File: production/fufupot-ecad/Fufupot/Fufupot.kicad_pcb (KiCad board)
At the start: 4 copper layers, 127 x 127 mm, 56 parts, among them IC1 FOD3150, J1 Conn_01x04, J10 Conn_01x03, J11 Conn_01x03, J12 Conn_01x02, J13 Conn_01x03, J2 USB_B, J3 Conn_01x03, J4 Conn_01x02, J6 Conn_01x02, J7 Conn_01x02, J8 Conn_01x04, J9 Conn_01x02, SW1 SW_Push, SW2 SW_Push, U1 USBLC6-2SC6, U2 LM5165DRC, U3 FT232RL, U4 ATMEGA328P-PN, U5 STGP8NC60KD

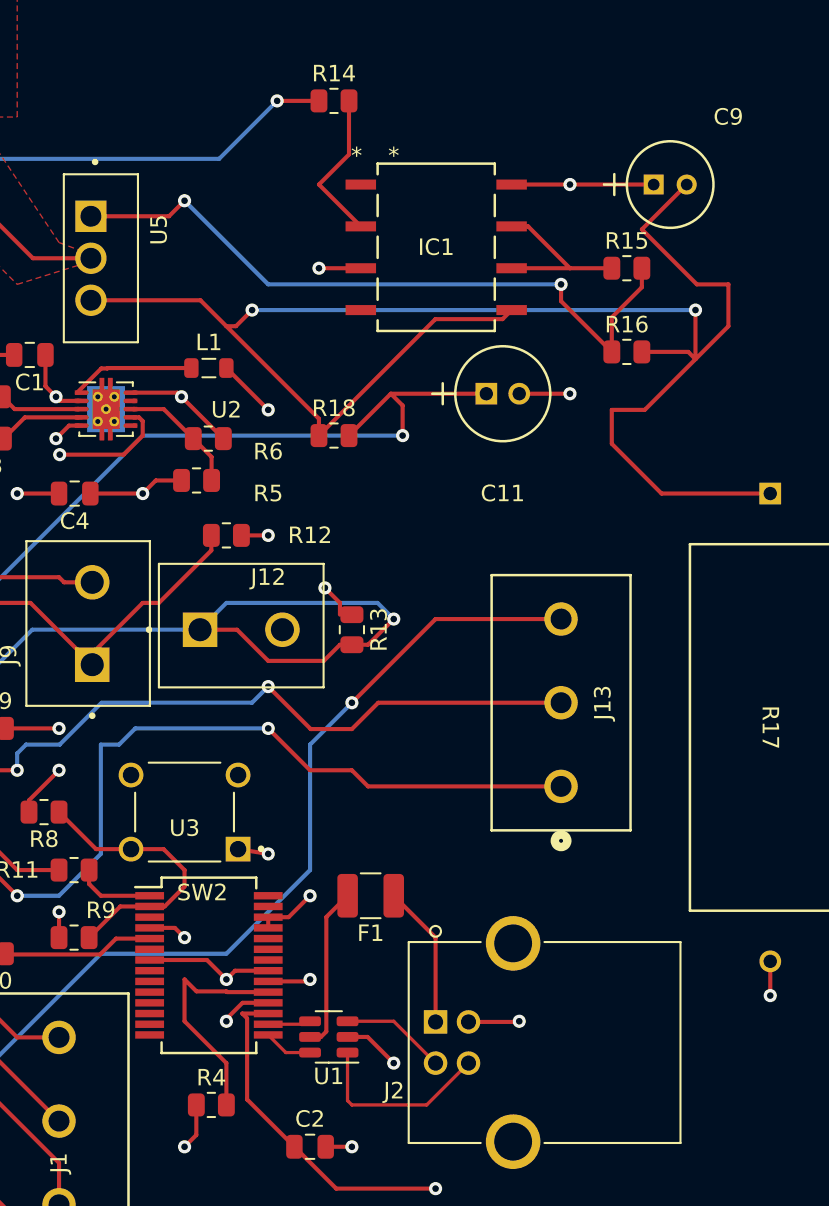
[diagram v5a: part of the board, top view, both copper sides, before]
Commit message: i hope it works! fixing routing
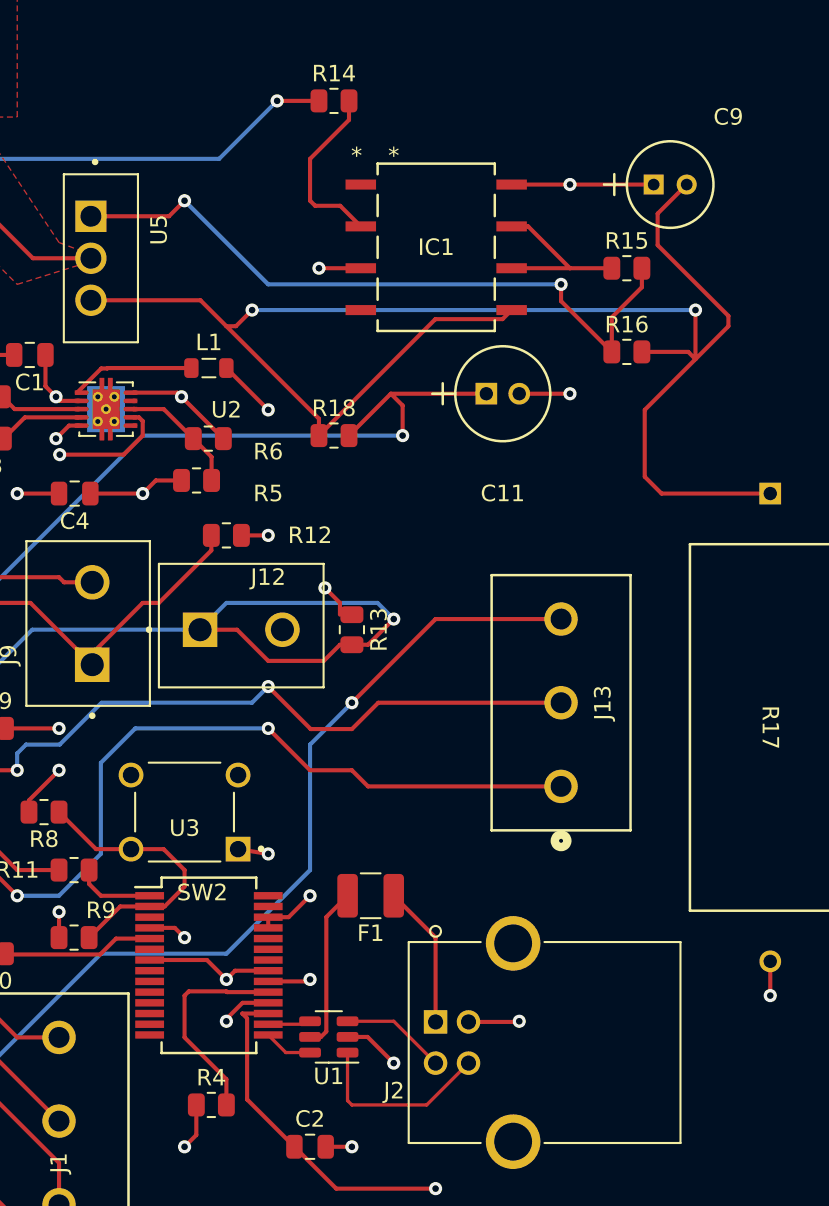
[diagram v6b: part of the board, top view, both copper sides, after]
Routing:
- net Net-(IC1-VSS): track 103.1 -> 98.4 mm
- net Net-(IC1-ANODE): track 9.43 -> 10.8 mm
- net Net-(U3-~{RESET}): track 14.1 -> 12.9 mm
- net A4: track 51.7 -> 51.0 mm
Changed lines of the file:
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@@
         (effects (font (size 1 1) (thickness 0.15)))
     )
-    (fp_text value "10k" (at 0 1.65) (layer "F.Fab")
+    (fp_text value "10k" (at 0 1.65) (layer "F.Fab") hide
         (effects (font (size 1 1) (thickness 0.15)))
     )
@@
   (via (at 104.14 106.68) (size 0.8) (drill 0.4) (layers "F.Cu" "B.Cu") (free) (net 6))
   (via (at 109.22 118.399415) (size 0.8) (drill 0.4) (layers "F.Cu" "B.Cu") (free) (net 6))
-  (segment (start 117.565 131.824415) (end 116.84 131.099415) (width 0.25) (layer "F.Cu") (net 7))
-  (segment (start 116.84 133.639415) (end 119.38 136.179415) (width 0.25) (layer "F.Cu") (net 7))
-  (segment (start 119.425 131.869415) (end 119.38 131.824415) (width 0.25) (layer "F.Cu") (net 7))
   (segment (start 121.92 131.869415) (end 119.425 131.869415) (width 0.25) (layer "F.Cu") (net 7))
-  (segment (start 119.38 136.179415) (end 119.38 138.719415) (width 0.25) (layer "F.Cu") (net 7))
-  (segment (start 116.84 131.099415) (end 116.84 133.639415) (width 0.25) (layer "F.Cu") (net 7))
-  (segment (start 119.38 131.824415) (end 117.565 131.824415) (width 0.25) (layer "F.Cu") (net 7))
+  (segment (start 119.38 131.824415) (end 117.095585 131.824415) (width 0.25) (layer "F.Cu") (net 7))
+  (segment (start 116.84 132.08) (end 116.84 134.62) (width 0.25) (layer "F.Cu") (net 7))
+  (segment (start 117.095585 131.824415) (end 116.84 132.08) (width 0.25) (layer "F.Cu") (net 7))
+  (segment (start 119.425 131.869415) (end 119.38 131.824415) (width 0.25) (layer "F.Cu") (net 7))
+  (segment (start 119.38 137.16) (end 119.38 138.719415) (width 0.25) (layer "F.Cu") (net 7))
+  (segment (start 116.84 134.62) (end 119.38 137.16) (width 0.25) (layer "F.Cu") (net 7))
   (segment (start 116.84 124.46) (end 116.84 125.459035) (width 0.25) (layer "F.Cu") (net 8))
   (segment (start 113.59 123.189415) (end 115.569415 123.189415) (width 0.25) (layer "F.Cu") (net 8))
@@
   (via (at 140.24 82.839415) (size 0.8) (drill 0.4) (layers "F.Cu" "B.Cu") (free) (net 36))
   (segment (start 136.697 90.459415) (end 136.1454 91.011015) (width 0.25) (layer "F.Cu") (net 37))
-  (segment (start 142.78 96.52) (end 142.78 98.579418) (width 0.25) (layer "F.Cu") (net 37))
-  (segment (start 147.943985 88.9) (end 149.86 88.9) (width 0.25) (layer "F.Cu") (net 37))
   (segment (start 125 97.06) (end 119.38 91.44) (width 0.25) (layer "F.Cu") (net 37))
   (segment (start 152.4 101.6) (end 145.800582 101.6) (width 0.25) (layer "F.Cu") (net 37))
@@
   (segment (start 125 98.079415) (end 125 97.06) (width 0.25) (layer "F.Cu") (net 37))
   (segment (start 136.1454 91.011015) (end 132.0684 91.011015) (width 0.25) (layer "F.Cu") (net 37))
+  (segment (start 144.78 100.579418) (end 145.800582 101.6) (width 0.25) (layer "F.Cu") (net 37))
+  (segment (start 145.563008 84.603008) (end 147.3266 82.839415) (width 0.25) (layer "F.Cu") (net 37))
   (segment (start 119.38 91.44) (end 117.804415 89.864415) (width 0.25) (layer "F.Cu") (net 37))
-  (segment (start 149.86 91.44) (end 147.86 93.44) (width 0.25) (layer "F.Cu") (net 37))
-  (segment (start 144.78 96.52) (end 142.78 96.52) (width 0.25) (layer "F.Cu") (net 37))
-  (segment (start 144.605 85.561015) (end 147.943985 88.9) (width 0.25) (layer "F.Cu") (net 37))
+  (segment (start 145.563008 86.519024) (end 145.563008 84.603008) (width 0.25) (layer "F.Cu") (net 37))
   (segment (start 147.419415 92.999415) (end 147.86 93.44) (width 0.25) (layer "F.Cu") (net 37))
   (segment (start 147.86 90.459415) (end 147.86 93.44) (width 0.25) (layer "F.Cu") (net 37))
-  (segment (start 149.86 88.9) (end 149.86 91.44) (width 0.25) (layer "F.Cu") (net 37))
   (segment (start 132.0684 91.011015) (end 125 98.079415) (width 0.25) (layer "F.Cu") (net 37))
   (segment (start 120.939415 90.459415) (end 119.95883 91.44) (width 0.25) (layer "F.Cu") (net 37))
-  (segment (start 145.800582 101.6) (end 142.78 98.579418) (width 0.25) (layer "F.Cu") (net 37))
+  (segment (start 149.86 90.816015) (end 145.563008 86.519024) (width 0.25) (layer "F.Cu") (net 37))
+  (segment (start 147.86 93.44) (end 149.86 91.44) (width 0.25) (layer "F.Cu") (net 37))
+  (segment (start 149.86 91.44) (end 149.86 90.816015) (width 0.25) (layer "F.Cu") (net 37))
   (segment (start 119.95883 91.44) (end 119.38 91.44) (width 0.25) (layer "F.Cu") (net 37))
-  (segment (start 144.605 85.561015) (end 147.3266 82.839415) (width 0.25) (layer "F.Cu") (net 37))
   (segment (start 144.605 92.999415) (end 147.419415 92.999415) (width 0.25) (layer "F.Cu") (net 37))
+  (segment (start 144.78 96.52) (end 144.78 100.579418) (width 0.25) (layer "F.Cu") (net 37))
   (segment (start 117.804415 89.864415) (end 111.155 89.864415) (width 0.25) (layer "F.Cu") (net 37))
   (via (at 147.86 90.459415) (size 0.8) (drill 0.4) (layers "F.Cu" "B.Cu") (free) (net 37))
@@
   (segment (start 114.3 98.079415) (end 130.08 98.079415) (width 0.25) (layer "B.Cu") (net 40))
   (segment (start 104.14 110.779415) (end 104.14 108.239415) (width 0.25) (layer "B.Cu") (net 40))
-  (segment (start 126.825 81.014415) (end 126.825 77.759415) (width 0.25) (layer "F.Cu") (net 42))
-  (segment (start 125 82.839415) (end 126.825 81.014415) (width 0.25) (layer "F.Cu") (net 42))
-  (segment (start 127.54 85.379415) (end 125 82.839415) (width 0.25) (layer "F.Cu") (net 42))
+  (segment (start 124.46 83.82) (end 124.46 81.28) (width 0.25) (layer "F.Cu") (net 42))
+  (segment (start 126.825 78.915) (end 126.825 77.759415) (width 0.25) (layer "F.Cu") (net 42))
+  (segment (start 127.54 85.379415) (end 126.2879 84.127316) (width 0.25) (layer "F.Cu") (net 42))
+  (segment (start 124.767316 84.127316) (end 124.46 83.82) (width 0.25) (layer "F.Cu") (net 42))
+  (segment (start 126.2879 84.127316) (end 124.767316 84.127316) (width 0.25) (layer "F.Cu") (net 42))
+  (segment (start 124.46 81.28) (end 126.825 78.915) (width 0.25) (layer "F.Cu") (net 42))
   (segment (start 137.7 85.379415) (end 140.24 87.919415) (width 0.25) (layer "F.Cu") (net 44))
   (segment (start 142.78 87.919415) (end 140.24 87.919415) (width 0.25) (layer "F.Cu") (net 44))
@@
   (via (at 121.92 115.859415) (size 0.8) (drill 0.4) (layers "F.Cu" "B.Cu") (free) (net 52))
   (via (at 106.68 126.019415) (size 0.8) (drill 0.4) (layers "F.Cu" "B.Cu") (free) (net 52))
-  (segment (start 113.85 115.859415) (end 121.92 115.859415) (width 0.25) (layer "B.Cu") (net 52))
-  (segment (start 112.869415 116.84) (end 113.85 115.859415) (width 0.25) (layer "B.Cu") (net 52))
-  (segment (start 111.76 123.479415) (end 111.76 116.84) (width 0.25) (layer "B.Cu") (net 52))
-  (segment (start 111.76 116.84) (end 112.869415 116.84) (width 0.25) (layer "B.Cu") (net 52))
-  (segment (start 109.22 126.019415) (end 111.76 123.479415) (width 0.25) (layer "B.Cu") (net 52))
   (segment (start 106.68 126.019415) (end 109.22 126.019415) (width 0.25) (layer "B.Cu") (net 52))
+  (segment (start 109.22 126.019415) (end 111.76 123.479415) (width 0.25) (layer "B.Cu") (net 52))
+  (segment (start 111.76 123.479415) (end 111.76 117.949415) (width 0.25) (layer "B.Cu") (net 52))
+  (segment (start 113.85 115.859415) (end 121.92 115.859415) (width 0.25) (layer "B.Cu") (net 52))
+  (segment (start 111.76 117.949415) (end 113.85 115.859415) (width 0.25) (layer "B.Cu") (net 52))
   (segment (start 128.599415 114.3) (end 139.7 114.3) (width 0.25) (layer "F.Cu") (net 53))
   (segment (start 127 115.899415) (end 128.599415 114.3) (width 0.25) (layer "F.Cu") (net 53))

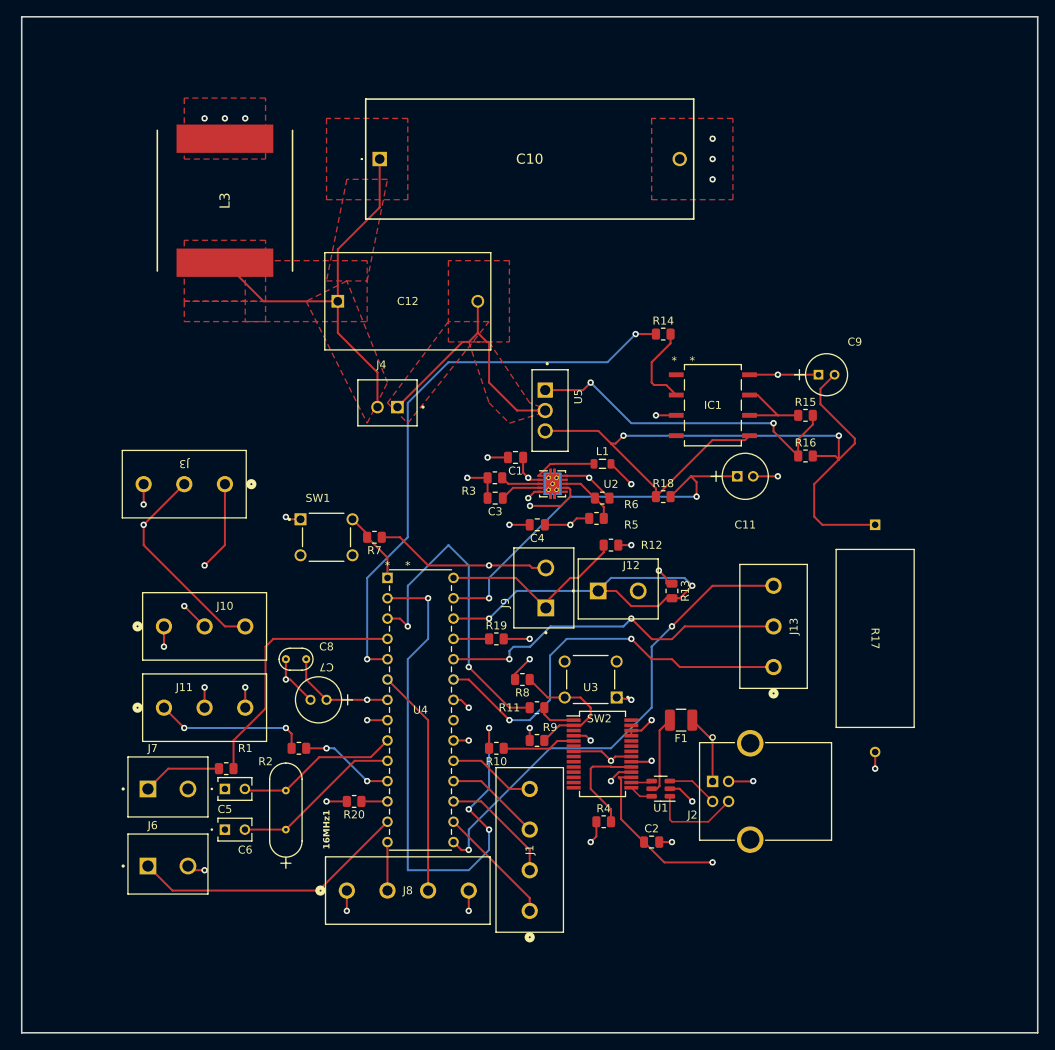
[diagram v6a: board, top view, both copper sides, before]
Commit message: Added Mounting Holes
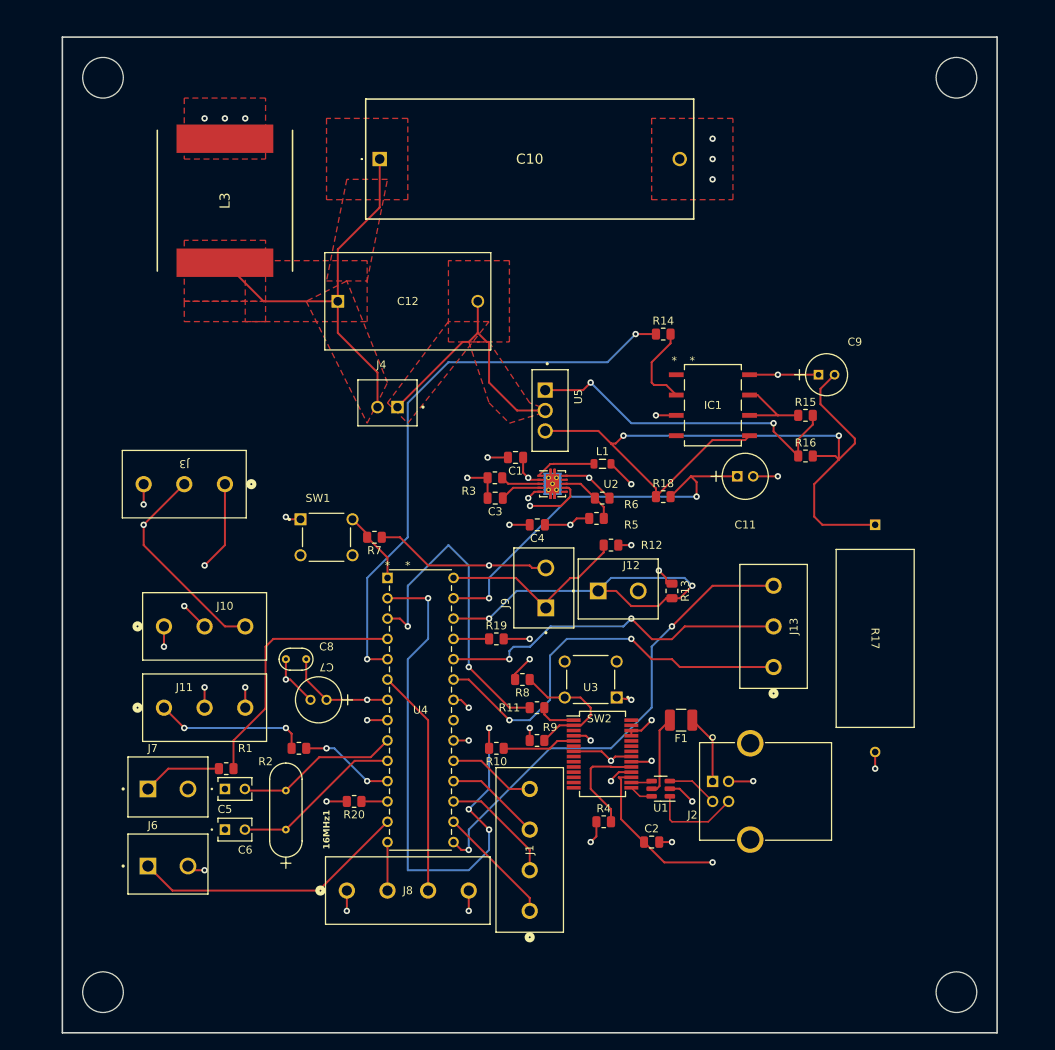
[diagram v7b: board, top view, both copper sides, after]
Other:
- board size 127 x 127 mm -> 116.8 x 124.5 mm
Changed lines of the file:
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@@
     )
   )
-  (gr_rect (start 45.72 38.1) (end 172.72 165.1)
+  (gr_circle (center 55.88 45.72) (end 53.34 45.72)
+    (stroke (width 0.1) (type default)) (fill none) (layer "Edge.Cuts"))
+  (gr_circle (center 55.88 160.02) (end 53.34 160.02)
+    (stroke (width 0.1) (type default)) (fill none) (layer "Edge.Cuts"))
+  (gr_circle (center 162.56 160.02) (end 160.02 160.02)
+    (stroke (width 0.1) (type default)) (fill none) (layer "Edge.Cuts"))
+  (gr_circle (center 162.56 45.72) (end 160.02 45.72)
+    (stroke (width 0.1) (type default)) (fill none) (layer "Edge.Cuts"))
+  (gr_rect (start 50.8 40.64) (end 167.64 165.1)
     (stroke (width 0.2) (type default)) (fill none) (layer "Edge.Cuts"))
   (segment (start 120.346776 133.169415) (end 120.637156 133.459795) (width 0.25) (layer "F.Cu") (net 1))
@@
     (polygon
       (pts
-        (xy 58.42 45.72)
-        (xy 167.64 45.72)
-        (xy 167.64 152.4)
-        (xy 58.42 152.4)
+        (xy 50.8 40.64)
+        (xy 167.64 40.64)
+        (xy 167.64 165.1)
+        (xy 50.8 165.1)
       )
     )
@@
     (polygon
       (pts
-        (xy 111.76 45.72)
-        (xy 167.64 45.72)
+        (xy 111.76 40.64)
+        (xy 167.64 40.64)
         (xy 167.64 104.14)
         (xy 111.76 104.14)
@@
     (polygon
       (pts
-        (xy 58.42 104.14)
+        (xy 50.8 104.14)
         (xy 127 104.14)
-        (xy 127 152.4)
-        (xy 58.42 152.4)
+        (xy 127 165.1)
+        (xy 50.8 165.1)
       )
     )
@@
     (polygon
       (pts
-        (xy 58.42 45.72)
-        (xy 58.42 104.14)
+        (xy 50.8 40.64)
+        (xy 50.8 104.14)
         (xy 111.76 104.14)
-        (xy 111.76 45.72)
-      )
-    )
+        (xy 111.76 40.64)
+      )
+    )
